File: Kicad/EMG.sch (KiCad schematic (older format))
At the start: 0 parts

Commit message: Agregado componente OPA4243 y ubicación en esquemático
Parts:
- added U? (x4): OPA4243, symbol OPA4243
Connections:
- wire segments 0 -> 12
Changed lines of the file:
@@
 EESchema Schematic File Version 2
+LIBS:conn
+LIBS:device
+LIBS:Gajda_amplif
+LIBS:opa4243
+EELAYER 25 0
+EELAYER END
+$Descr A4 11693 8268
+encoding utf-8
+Sheet 1 1
+Title ""
+Date ""
+Rev ""
+Comp ""
+Comment1 ""
+Comment2 ""
+Comment3 ""
+Comment4 ""
+$EndDescr
+$Comp
+L OPA4243 U?
+U 1 1 57D57323
+P 1700 1400
+F 0 "U?" H 1850 1600 60  0000 C CNN
+F 1 "OPA4243" H 1950 1200 60  0000 C CNN
+F 2 "" H 1700 1400 60  0000 C CNN
+F 3 "" H 1700 1400 60  0000 C CNN
+	1    1700 1400
+	1    0    0    -1
+$EndComp
+$Comp
+L OPA4243 U?
+U 2 1 57D5736A
+P 1700 2450
+F 0 "U?" H 1850 2650 60  0000 C CNN
+F 1 "OPA4243" H 1950 2250 60  0000 C CNN
+F 2 "" H 1700 2450 60  0000 C CNN
+F 3 "" H 1700 2450 60  0000 C CNN
+	2    1700 2450
+	1    0    0    -1
+$EndComp
+$Comp
+L OPA4243 U?
+U 3 1 57D573C9
+P 1700 3400
+F 0 "U?" H 1850 3600 60  0000 C CNN
+F 1 "OPA4243" H 1950 3200 60  0000 C CNN
+F 2 "" H 1700 3400 60  0000 C CNN
+F 3 "" H 1700 3400 60  0000 C CNN
+	3    1700 3400
+	1    0    0    -1
+$EndComp
+$Comp
+L OPA4243 U?
+U 4 1 57D57404
+P 3100 2450
+F 0 "U?" H 3250 2650 60  0000 C CNN
+F 1 "OPA4243" H 3350 2250 60  0000 C CNN
+F 2 "" H 3100 2450 60  0000 C CNN
+F 3 "" H 3100 2450 60  0000 C CNN
+	4    3100 2450
+	1    0    0    -1
+$EndComp
+Wire Wire Line
+	1350 1500 1350 1850
+Wire Wire Line
+	1350 1850 2050 1850
+Wire Wire Line
+	2050 1850 2050 1400
+Wire Wire Line
+	1350 2550 1350 2900
+Wire Wire Line
+	1350 2900 2050 2900
+Wire Wire Line
+	2050 2900 2050 2450
+Wire Wire Line
+	1350 3500 1350 3850
+Wire Wire Line
+	1350 3850 2050 3850
+Wire Wire Line
+	2050 3850 2050 3400
+Wire Wire Line
+	2050 2450 2300 2450
+Wire Wire Line
+	2300 2450 2300 2350
+Wire Wire Line
+	2300 2350 2750 2350
+$EndSCHEMATC

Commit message: Creada librería TLC2274
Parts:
- removed U? (x4): OPA4243, symbol OPA4243
- added U? (x4): TLC2274, symbol TLC2274
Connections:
- wire segments 12 -> 0
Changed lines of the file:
@@
 LIBS:Gajda_amplif
 LIBS:opa4243
+LIBS:tlc2274
+LIBS:EMG-cache
 EELAYER 25 0
 EELAYER END
@@
 $EndDescr
 $Comp
-L OPA4243 U?
-U 1 1 57D57323
-P 1700 1400
-F 0 "U?" H 1850 1600 60  0000 C CNN
-F 1 "OPA4243" H 1950 1200 60  0000 C CNN
-F 2 "" H 1700 1400 60  0000 C CNN
-F 3 "" H 1700 1400 60  0000 C CNN
-	1    1700 1400
+L TLC2274 U?
+U 1 1 57D7298D
+P 2350 1900
+F 0 "U?" H 2500 2100 60  0000 C CNN
+F 1 "TLC2274" H 2600 1700 60  0000 C CNN
+F 2 "" H 2350 1900 60  0000 C CNN
+F 3 "" H 2350 1900 60  0000 C CNN
+	1    2350 1900
 	1    0    0    -1
 $EndComp
 $Comp
-L OPA4243 U?
-U 2 1 57D5736A
-P 1700 2450
-F 0 "U?" H 1850 2650 60  0000 C CNN
-F 1 "OPA4243" H 1950 2250 60  0000 C CNN
-F 2 "" H 1700 2450 60  0000 C CNN
-F 3 "" H 1700 2450 60  0000 C CNN
-	2    1700 2450
+L TLC2274 U?
+U 2 1 57D729BC
+P 2350 3200
+F 0 "U?" H 2500 3400 60  0000 C CNN
+F 1 "TLC2274" H 2600 3000 60  0000 C CNN
+F 2 "" H 2350 3200 60  0000 C CNN
+F 3 "" H 2350 3200 60  0000 C CNN
+	2    2350 3200
 	1    0    0    -1
 $EndComp
 $Comp
-L OPA4243 U?
-U 3 1 57D573C9
-P 1700 3400
-F 0 "U?" H 1850 3600 60  0000 C CNN
-F 1 "OPA4243" H 1950 3200 60  0000 C CNN
-F 2 "" H 1700 3400 60  0000 C CNN
-F 3 "" H 1700 3400 60  0000 C CNN
-	3    1700 3400
+L TLC2274 U?
+U 3 1 57D729DF
+P 4400 1900
+F 0 "U?" H 4550 2100 60  0000 C CNN
+F 1 "TLC2274" H 4650 1700 60  0000 C CNN
+F 2 "" H 4400 1900 60  0000 C CNN
+F 3 "" H 4400 1900 60  0000 C CNN
+	3    4400 1900
 	1    0    0    -1
 $EndComp
 $Comp
-L OPA4243 U?
-U 4 1 57D57404
-P 3100 2450
-F 0 "U?" H 3250 2650 60  0000 C CNN
-F 1 "OPA4243" H 3350 2250 60  0000 C CNN
-F 2 "" H 3100 2450 60  0000 C CNN
-F 3 "" H 3100 2450 60  0000 C CNN
-	4    3100 2450
+L TLC2274 U?
+U 4 1 57D72A66
+P 4400 3200
+F 0 "U?" H 4550 3400 60  0000 C CNN
+F 1 "TLC2274" H 4650 3000 60  0000 C CNN
+F 2 "" H 4400 3200 60  0000 C CNN
+F 3 "" H 4400 3200 60  0000 C CNN
+	4    4400 3200
 	1    0    0    -1
 $EndComp
-Wire Wire Line
-	1350 1500 1350 1850
-Wire Wire Line
-	1350 1850 2050 1850
-Wire Wire Line
-	2050 1850 2050 1400
-Wire Wire Line
-	1350 2550 1350 2900
-Wire Wire Line
-	1350 2900 2050 2900
-Wire Wire Line
-	2050 2900 2050 2450
-Wire Wire Line
-	1350 3500 1350 3850
-Wire Wire Line
-	1350 3850 2050 3850
-Wire Wire Line
-	2050 3850 2050 3400
-Wire Wire Line
-	2050 2450 2300 2450
-Wire Wire Line
-	2300 2450 2300 2350
-Wire Wire Line
-	2300 2350 2750 2350
 $EndSCHEMATC

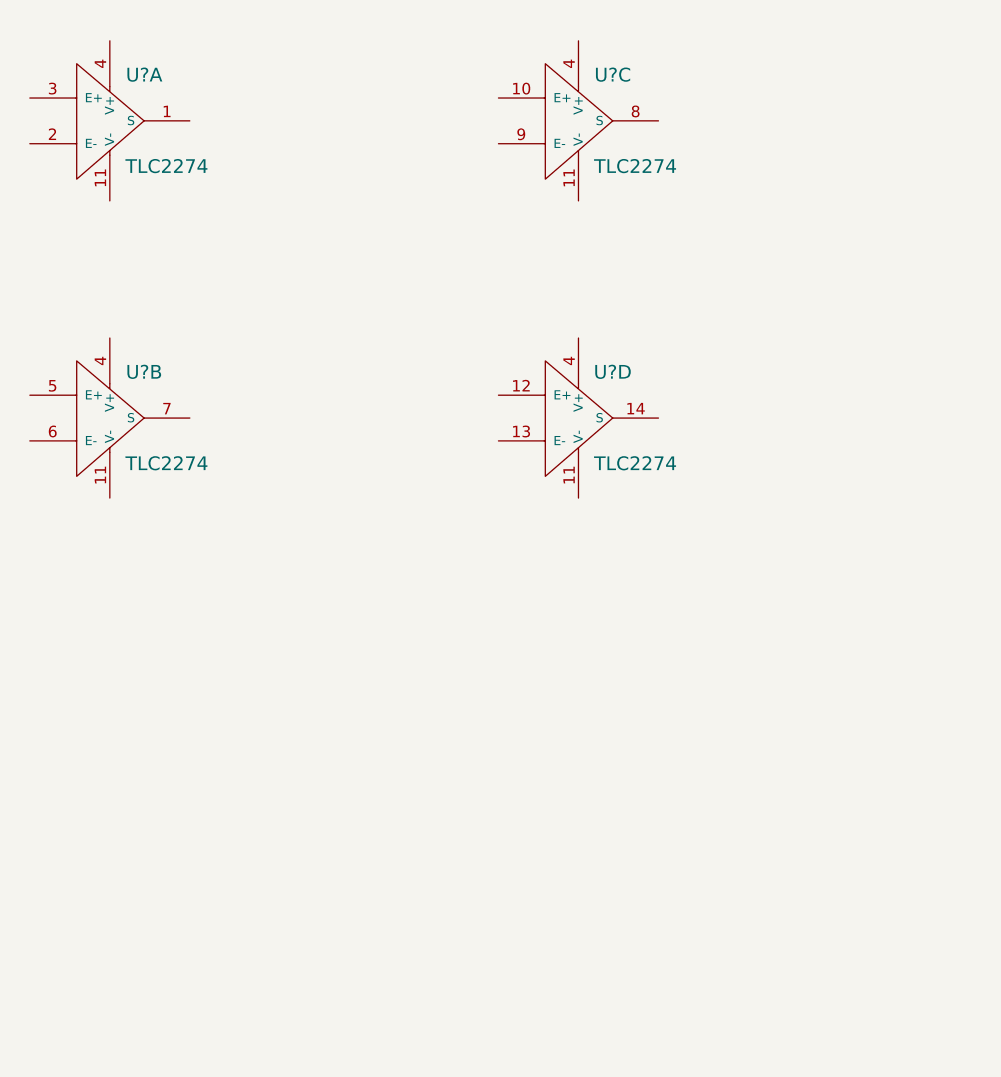
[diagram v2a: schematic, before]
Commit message: Agregada librería power y actualizado esquemático con circuito de adquisición
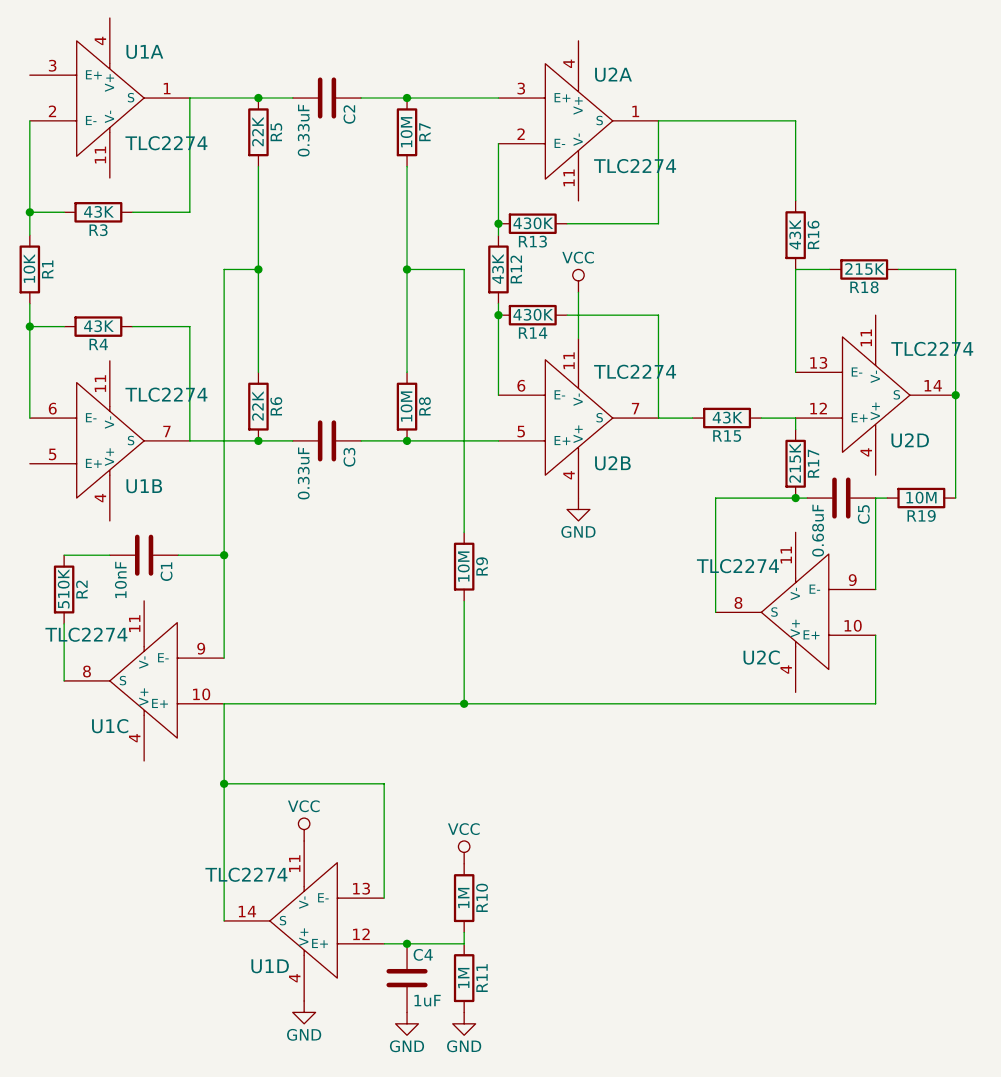
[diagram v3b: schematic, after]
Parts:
- added C1: 10nF, symbol C
- added C2, C3: 0.33uF, symbol C
- added C4: 1uF, symbol C
- added C5: 0.68uF, symbol C
- added R1: 10K, symbol R
- added R10, R11: 1M, symbol R
- added R12, R15, R16, R3, R4: 43K, symbol R
- added R13, R14: 430K, symbol R
- added R17, R18: 215K, symbol R
- added R19, R7, R8, R9: 10M, symbol R
- added R2: 510K, symbol R
- added R5, R6: 22K, symbol R
- added unit 3 of U1
- added unit 4 of U1
- added unit 4 of U2
- added unit 3 of U2
- gave numbers to parts that had none: 2
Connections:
- net at U1.1 (S): now also C2.2, R3.1, R5.1
- net at U1.2 (E-): now also R1.1, R3.2
- net at U1.6 (E-): now also R1.2, R4.2
- net at U1.7 (S): now also C3.2, R4.1, R6.2
- net VCC: now reaches U2.11 (V-)
- net VCC: now also R10.1, U1.11 (V-)
- net GND: now reaches U2.4 (V+)
- net GND: now also C4.2, R11.2, U1.4 (V+)
- new net: R13.1, R16.1, U2.1 (S)
- new net: R12.1, R13.2, U2.2 (E-)
- new net: C2.1, R7.1, U2.3 (E+)
- new net: C3.1, R8.2, U2.5 (E+)
- new net: R12.2, R14.2, U2.6 (E-)
- new net: R14.1, R15.2, U2.7 (S)
- new net: C1.1, R5.2, R6.1, U1.9 (E-)
- new net: R7.2, R8.1, R9.1
- new net: R15.1, R17.1, U2.12 (E+)
- new net: R16.2, R18.2, U2.13 (E-)
- new net: R18.1, R19.1, U2.14 (S)
- new net: C5.2, R17.2, U2.8 (S)
- new net: C5.1, R19.2, U2.9 (E-)
- new net: R9.2, U1.10 (E+), U1.13 (E-), U1.14 (S), U2.10 (E+)
- new net: R2.2, U1.8 (S)
- new net: C1.2, R2.1
- new net: C4.1, R10.2, R11.1, U1.12 (E+)
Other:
- moved on the sheet: U1A, U1B

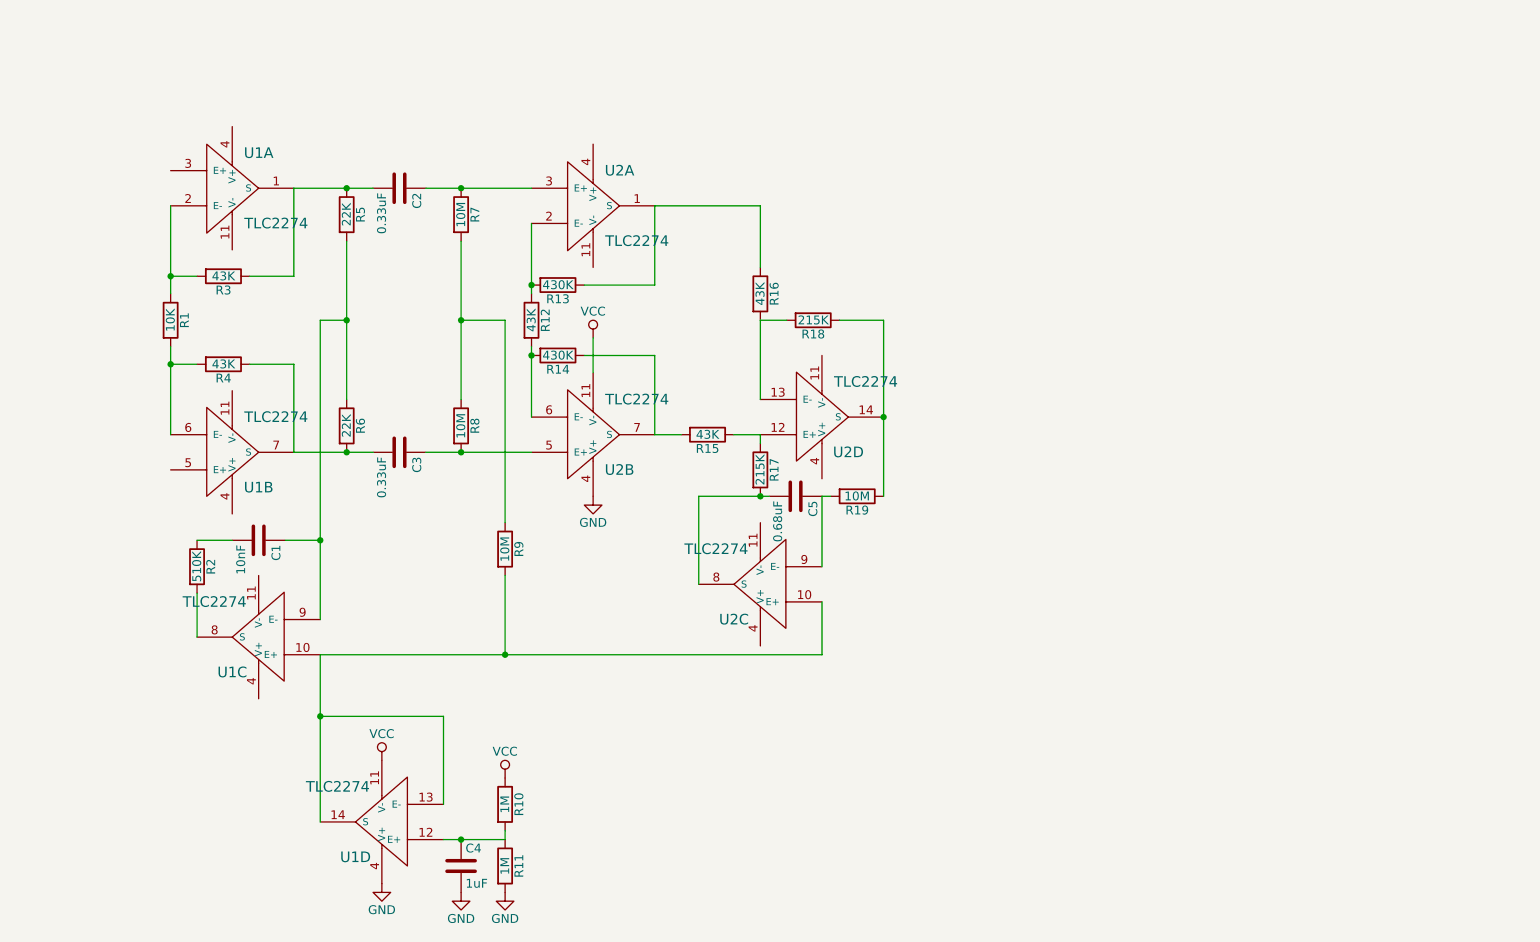
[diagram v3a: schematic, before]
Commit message: División del esquemático en hojas jerárquicas y etapas de adquisición y transmisión completas.
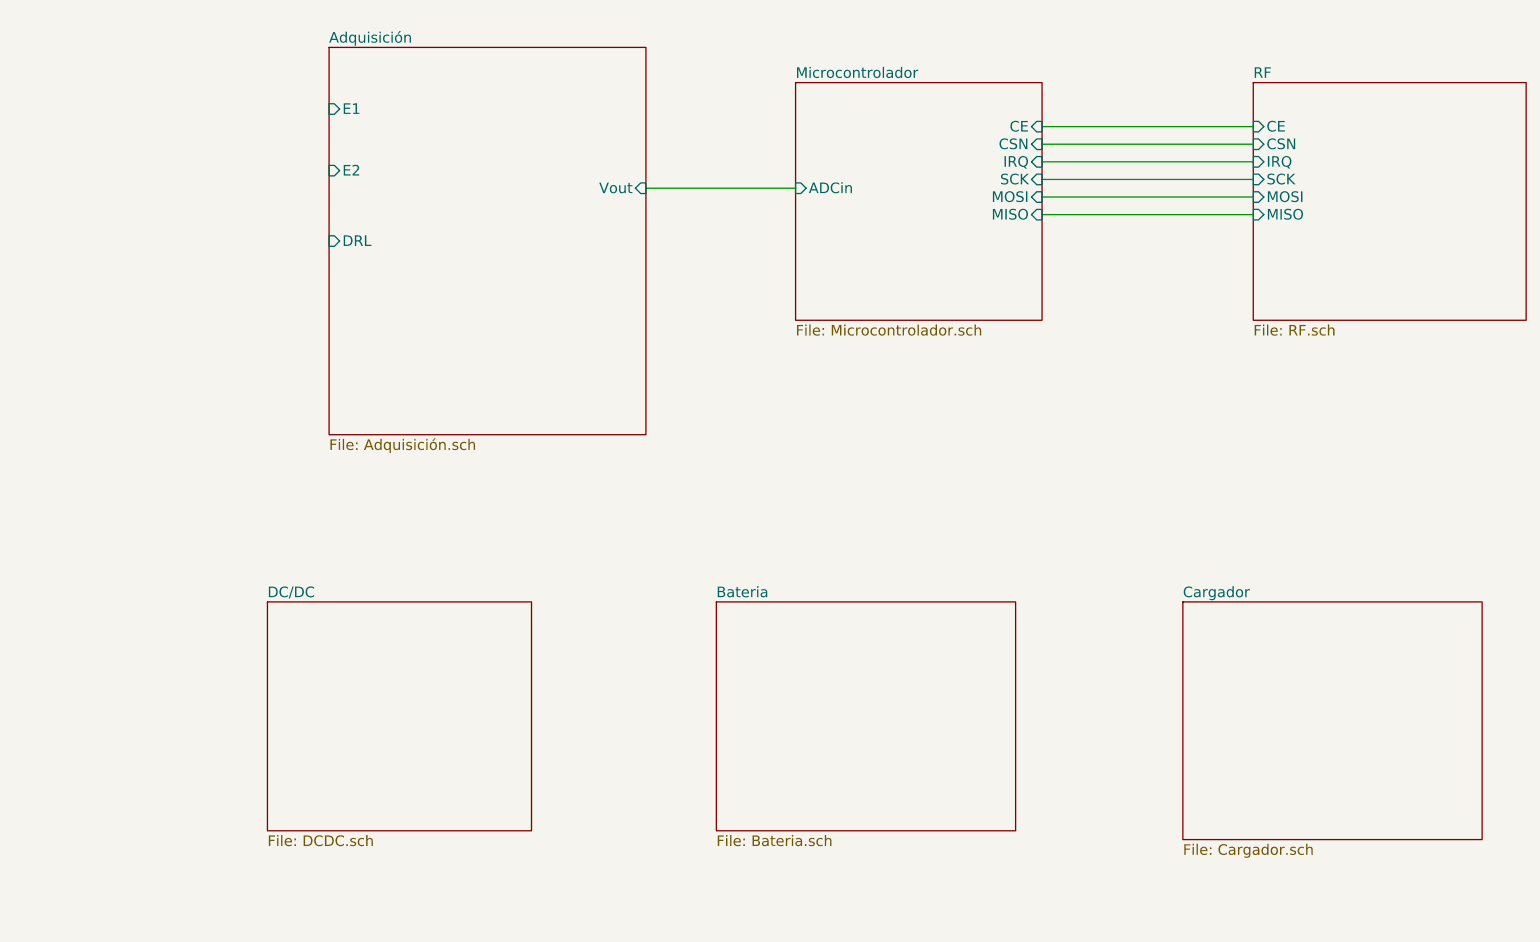
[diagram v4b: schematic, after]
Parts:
- removed C1: 10nF, symbol C
- removed C2, C3: 0.33uF, symbol C
- removed C4: 1uF, symbol C
- removed C5: 0.68uF, symbol C
- removed R1: 10K, symbol R
- removed R10, R11: 1M, symbol R
- removed R12, R15, R16, R3, R4: 43K, symbol R
- removed R13, R14: 430K, symbol R
- removed R17, R18: 215K, symbol R
- removed R19, R7, R8, R9: 10M, symbol R
- removed R2: 510K, symbol R
- removed R5, R6: 22K, symbol R
- removed U1, U2: TLC2274, symbol TLC2274

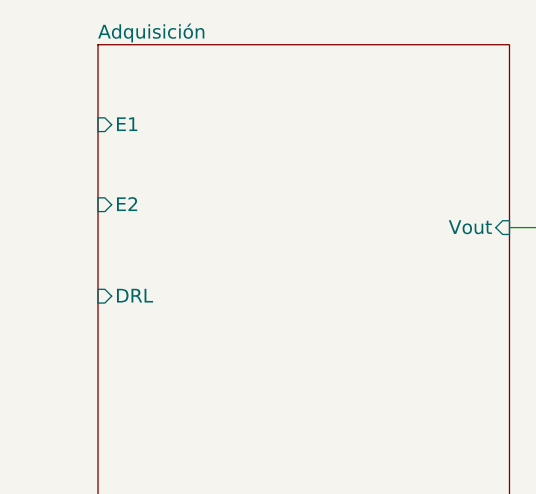
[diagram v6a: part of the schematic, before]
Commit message: Agregados footprints de pin headers para elementos faltantes (falta USB)
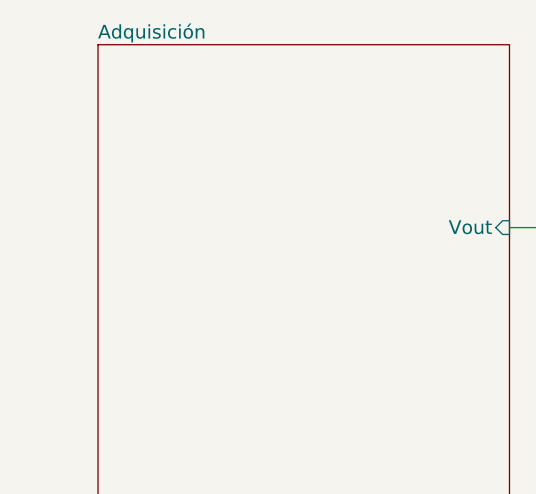
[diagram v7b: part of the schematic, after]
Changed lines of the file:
@@
 F0 "Adquisición" 60
 F1 "Adquisición.sch" 60
-F2 "E1" I L 2900 1350 60
-F3 "E2" I L 2900 1700 60
-F4 "DRL" I L 2900 2100 60
-F5 "Vout" I R 4700 1800 60
+F2 "Vout" I R 4700 1800 60
 $EndSheet
 $Sheet
